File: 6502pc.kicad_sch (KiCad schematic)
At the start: 41 parts, among them J1 DB9 Serial Port, J2 USB_B, J3 Conn_01x08_Pin, J4 Conn_01x08_Pin, J5 Conn_01x16_Socket, J6 SD-Card Board, J7 FTDI Socket, SW1 Reset Switch, SW2 SW_SPST, U1 W65C02SxP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

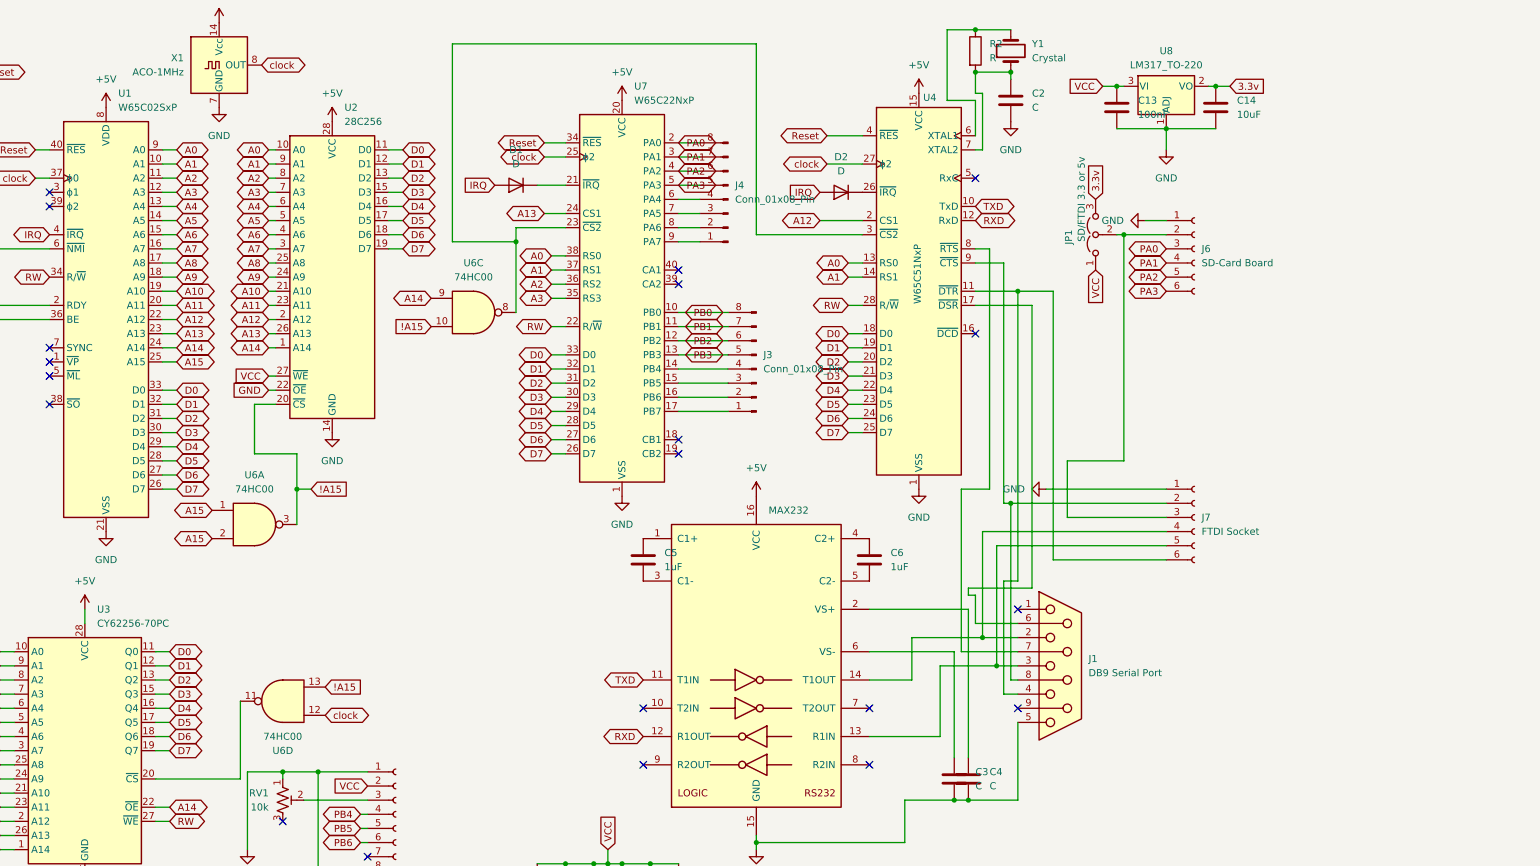
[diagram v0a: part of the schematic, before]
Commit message: Added Expansion
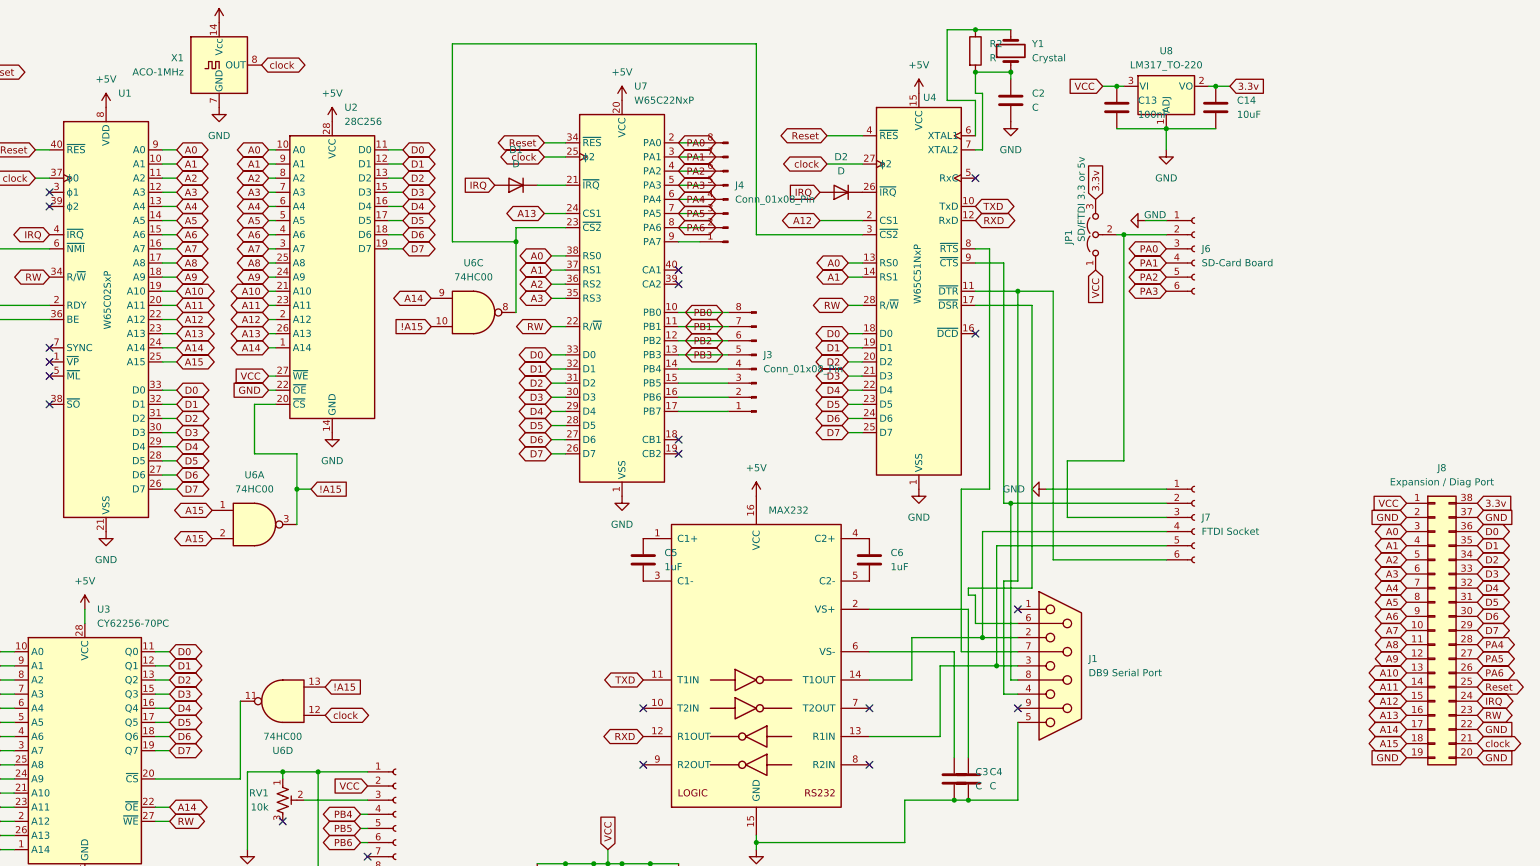
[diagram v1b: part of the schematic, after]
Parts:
- added J8: Expansion / Diag Port, Connector_PinHeader_2.54mm:PinHeader_2x19_P2.54mm_Vertical, symbol Connector_Generic:Conn_02x19_Counter_Clockwise
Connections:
- net +5V: now also J8.1 (Pin_1)
- net 3.3v: now also J8.38 (Pin_38)
- net A0: now also J8.3 (Pin_3)
- net A1: now also J8.4 (Pin_4)
- net A10: now also J8.13 (Pin_13)
- net A11: now also J8.14 (Pin_14)
- net A12: now also J8.15 (Pin_15)
- net A13: now also J8.16 (Pin_16)
- net A14: now also J8.17 (Pin_17)
- net A15: now also J8.18 (Pin_18)
- net A2: now also J8.5 (Pin_5)
- net A3: now also J8.6 (Pin_6)
- net A4: now also J8.7 (Pin_7)
- net A5: now also J8.8 (Pin_8)
- net A6: now also J8.9 (Pin_9)
- net A7: now also J8.10 (Pin_10)
- net A8: now also J8.11 (Pin_11)
- net A9: now also J8.12 (Pin_12)
- net D0: now also J8.36 (Pin_36)
- net D1: now also J8.35 (Pin_35)
- net D2: now also J8.34 (Pin_34)
- net D3: now also J8.33 (Pin_33)
- net D4: now also J8.32 (Pin_32)
- net D5: now also J8.31 (Pin_31)
- net D6: now also J8.30 (Pin_30)
- net D7: now also J8.29 (Pin_29)
- net GND: now also J8.19 (Pin_19), J8.2 (Pin_2), J8.20 (Pin_20), J8.22 (Pin_22), J8.37 (Pin_37)
- net IRQ: now also J8.24 (Pin_24)
- net RW: now also J8.23 (Pin_23)
- net Reset: now also J8.25 (Pin_25)
- net clock: now also J8.21 (Pin_21)
- net PA4: now reaches J4.4 (Pin_4), U7.6 (PA4)
- net PA4: now also J8.28 (Pin_28)
- net PA5: now reaches J4.3 (Pin_3), U7.7 (PA5)
- net PA5: now also J8.27 (Pin_27)
- net PA6: now reaches J4.2 (Pin_2), U7.8 (PA6)
- net PA6: now also J8.26 (Pin_26)

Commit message: Added Expansion
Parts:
- J3, J4: footprint Connector_PinHeader_2.00mm:PinHeader_1x08_P2.00mm_Vertical -> Connector_PinHeader_2.54mm:PinHeader_1x08_P2.54mm_Vertical
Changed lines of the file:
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@@
 			)
 		)
-		(property "Footprint" "Connector_PinHeader_2.00mm:PinHeader_1x08_P2.00mm_Vertical"
+		(property "Footprint" "Connector_PinHeader_2.54mm:PinHeader_1x08_P2.54mm_Vertical"
 			(at 256.54 118.11 0)
 			(effects
@@
 			)
 		)
-		(property "Footprint" "Connector_PinHeader_2.00mm:PinHeader_1x08_P2.00mm_Vertical"
+		(property "Footprint" "Connector_PinHeader_2.54mm:PinHeader_1x08_P2.54mm_Vertical"
 			(at 251.46 87.63 0)
 			(effects

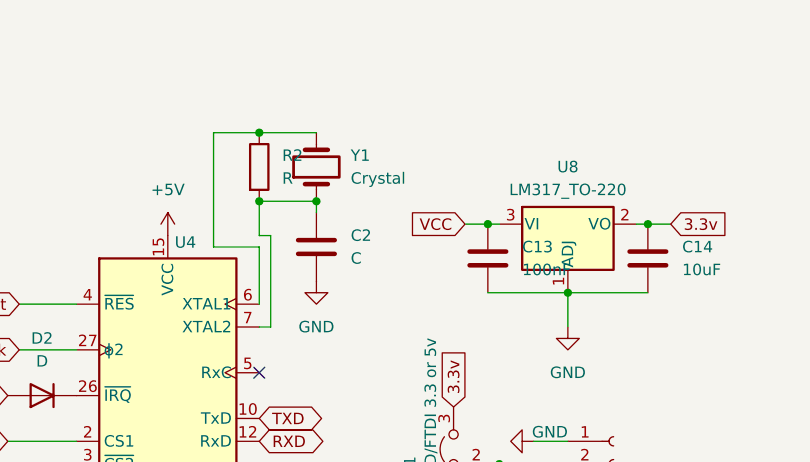
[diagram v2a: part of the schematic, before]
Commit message: Added Expansion
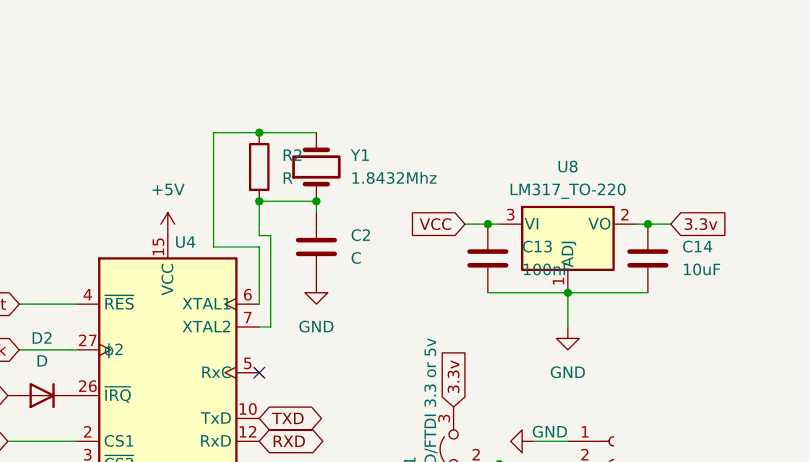
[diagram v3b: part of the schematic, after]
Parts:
- D1, D2: footprint Diode_THT:D_DO-15_P5.08mm_Vertical_AnodeUp -> Resistor_THT:R_Axial_DIN0204_L3.6mm_D1.6mm_P7.62mm_Horizontal
- R3: footprint Resistor_THT:R_Axial_DIN0204_L3.6mm_D1.6mm_P5.08mm_Horizontal -> Resistor_THT:R_Axial_DIN0204_L3.6mm_D1.6mm_P7.62mm_Horizontal
- RV1: footprint Potentiometer_THT:Potentiometer_Runtron_RM-063_Horizontal -> Potentiometer_THT:Potentiometer_Bourns_3296X_Horizontal
- Y1: value Crystal -> 1.8432Mhz; footprint Crystal:Crystal_HC18-U_Horizontal -> Crystal:Crystal_HC18-U_Vertical
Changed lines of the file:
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@@
 			)
 		)
-		(property "Footprint" "Diode_THT:D_DO-15_P5.08mm_Vertical_AnodeUp"
+		(property "Footprint" "Resistor_THT:R_Axial_DIN0204_L3.6mm_D1.6mm_P7.62mm_Horizontal"
 			(at 213.36 85.09 0)
 			(effects
@@
 			)
 		)
-		(property "Footprint" "Diode_THT:D_DO-15_P5.08mm_Vertical_AnodeUp"
+		(property "Footprint" "Resistor_THT:R_Axial_DIN0204_L3.6mm_D1.6mm_P7.62mm_Horizontal"
 			(at 271.78 86.36 0)
 			(effects
@@
 			)
 		)
-		(property "Footprint" "Resistor_THT:R_Axial_DIN0204_L3.6mm_D1.6mm_P5.08mm_Horizontal"
+		(property "Footprint" "Resistor_THT:R_Axial_DIN0204_L3.6mm_D1.6mm_P7.62mm_Horizontal"
 			(at 88.392 167.64 90)
 			(effects
@@
 			)
 		)
-		(property "Footprint" "Potentiometer_THT:Potentiometer_Runtron_RM-063_Horizontal"
+		(property "Footprint" "Potentiometer_THT:Potentiometer_Bourns_3296X_Horizontal"
 			(at 171.45 195.58 0)
 			(effects
@@
 			)
 		)
-		(property "Value" "Crystal"
+		(property "Value" "1.8432Mhz"
 			(at 306.07 62.2299 90)
 			(effects
@@
 			)
 		)
-		(property "Footprint" "Crystal:Crystal_HC18-U_Horizontal"
+		(property "Footprint" "Crystal:Crystal_HC18-U_Vertical"
 			(at 302.26 60.96 0)
 			(effects

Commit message: Added Expansion
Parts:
- J3, J4: footprint Connector_PinHeader_2.54mm:PinHeader_1x08_P2.54mm_Vertical -> Connector_PinSocket_2.54mm:PinSocket_1x08_P2.54mm_Vertical
- J5: footprint Connector_PinHeader_2.54mm:PinHeader_1x16_P2.54mm_Vertical -> Connector_PinSocket_2.54mm:PinSocket_1x16_P2.54mm_Vertical
- J6: footprint Connector_PinHeader_2.54mm:PinHeader_1x06_P2.54mm_Vertical -> Connector_PinSocket_2.54mm:PinSocket_1x06_P2.54mm_Vertical
- J8: footprint Connector_PinHeader_2.54mm:PinHeader_2x19_P2.54mm_Vertical -> Connector_PinSocket_2.54mm:PinSocket_2x19_P2.54mm_Vertical
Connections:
- net PA5: now also J5.4 (Pin_4)
- net PA6: now also J5.5 (Pin_5)
- net PB0: now also J5.7 (Pin_7); no longer J5.11 (Pin_11)
- net PB1: now also J5.8 (Pin_8); no longer J5.12 (Pin_12)
- net PB2: now also J5.9 (Pin_9); no longer J5.13 (Pin_13)
- net PB3: now also J5.10 (Pin_10); no longer J5.14 (Pin_14)
- net PB4: now also J3.4 (Pin_4), J5.11 (Pin_11), U7.14 (PB4); no longer J5.4 (Pin_4)
- net PB5: now also J3.3 (Pin_3), J5.12 (Pin_12), U7.15 (PB5); no longer J5.5 (Pin_5)
- net PB6: now also J3.2 (Pin_2), J5.13 (Pin_13), U7.16 (PB6); no longer J5.6 (Pin_6)
- net PB7: now reaches J3.1 (Pin_1), U7.17 (PB7)
- net PB7: now also J5.14 (Pin_14)
- net PA7: now reaches J4.1 (Pin_1), U7.9 (PA7)
- net PA7: now also J5.6 (Pin_6)
- no-connect marks 28 -> 24
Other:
- note added: "6502 SBC Computer with SD Card / TFDI Serial / DB9 and Expansion Port (Tom Smith)"

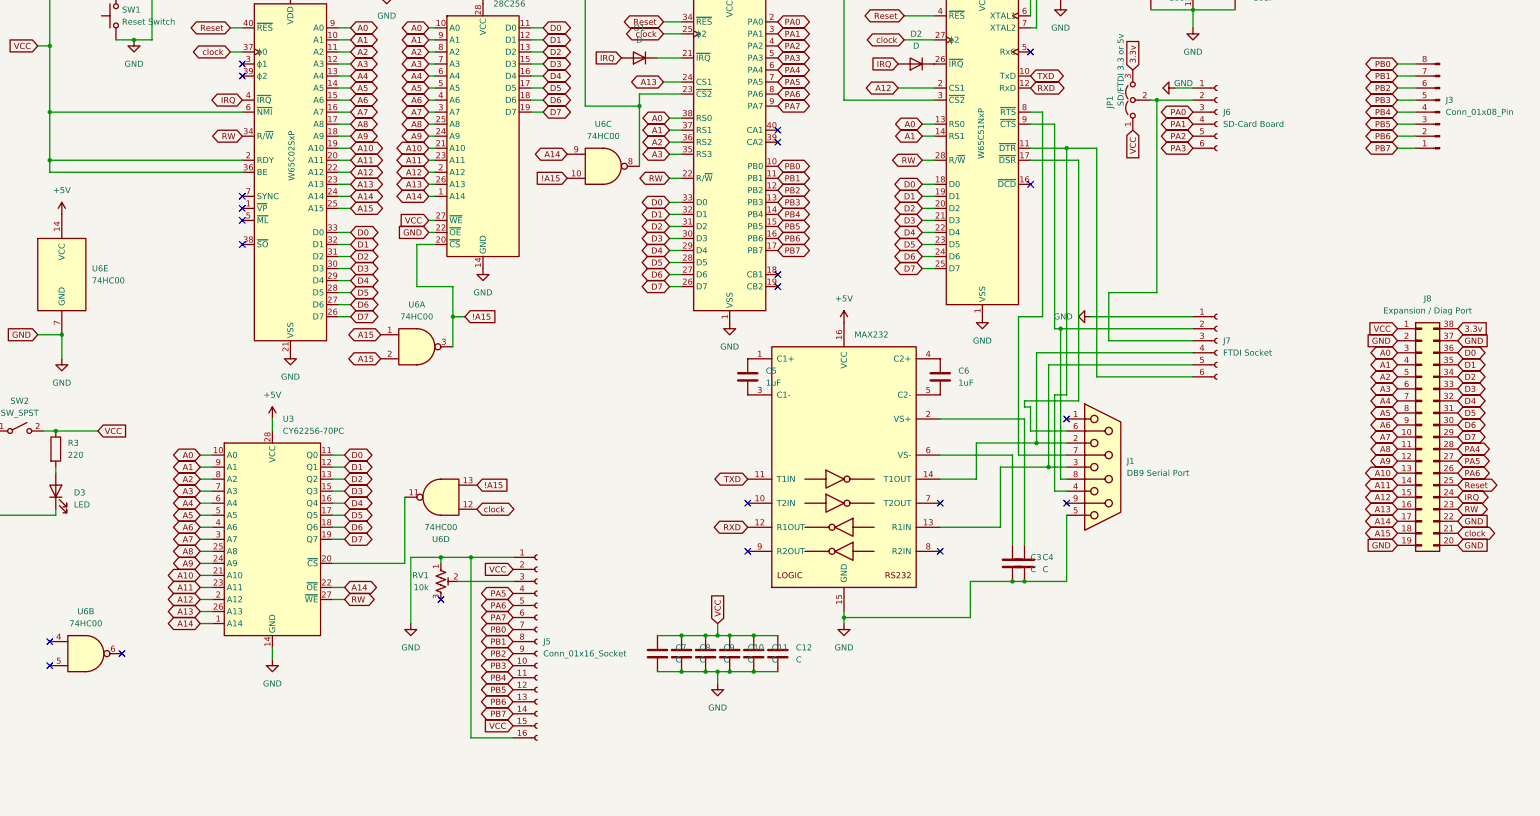
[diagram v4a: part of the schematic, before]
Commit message: Added Expansion
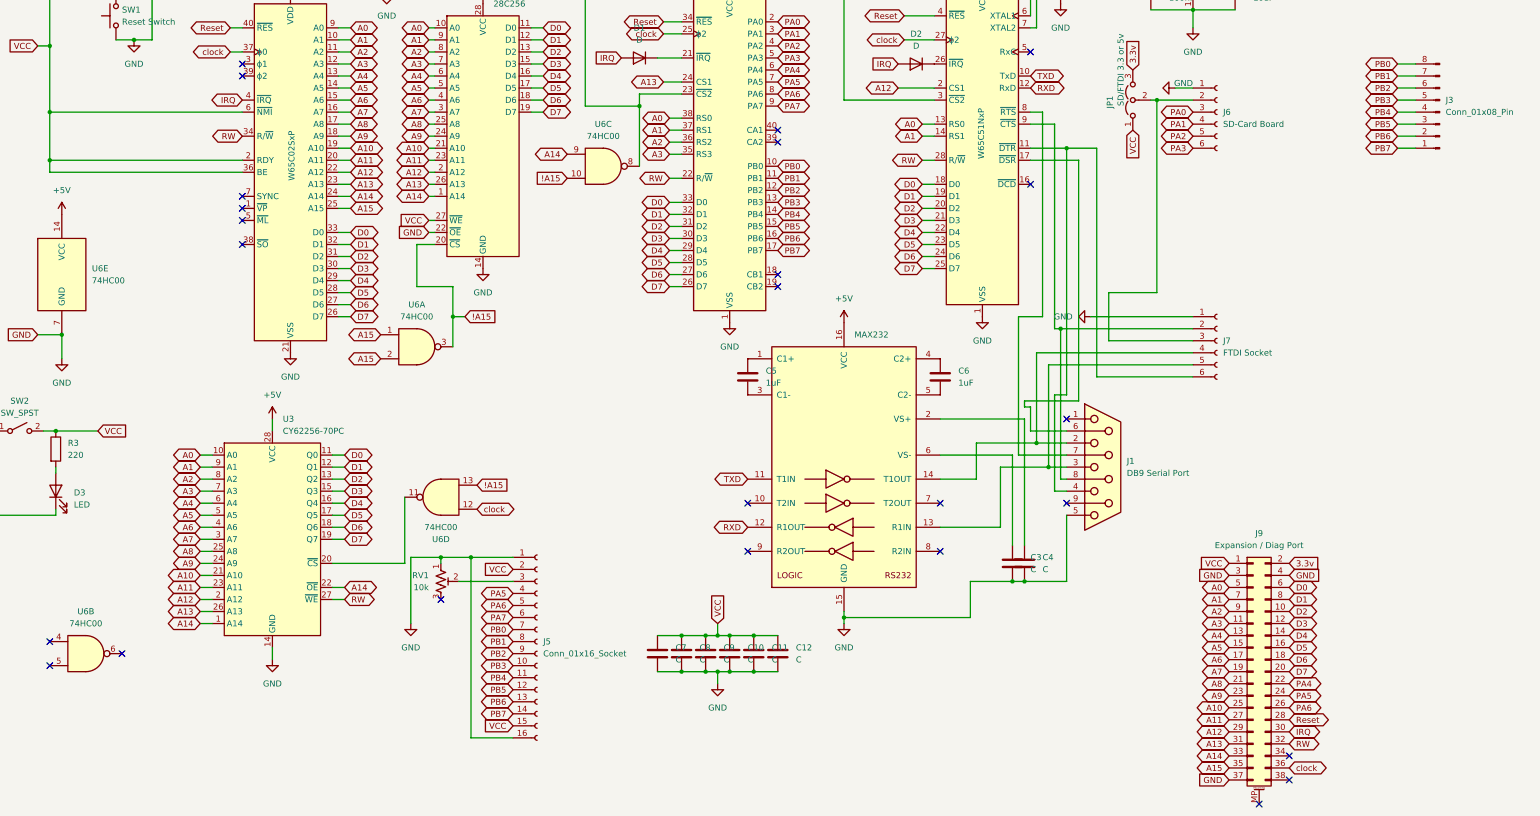
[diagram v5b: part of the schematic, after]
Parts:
- removed J8: Expansion / Diag Port, Connector_PinSocket_2.54mm:PinSocket_2x19_P2.54mm_Vertical, symbol Connector_Generic:Conn_02x19_Counter_Clockwise
- added J9: Expansion / Diag Port, Connector_PinHeader_2.54mm:PinHeader_2x19_P2.54mm_Vertical, symbol Connector_Generic_MountingPin:Conn_02x19_Odd_Even_MountingPin
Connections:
- net +5V: now also J9.1 (Pin_1)
- net 3.3v: now also J9.2 (Pin_2)
- net A0: now also J9.5 (Pin_5)
- net A1: now also J9.7 (Pin_7)
- net A10: now also J9.25 (Pin_25)
- net A11: now also J9.27 (Pin_27)
- net A12: now also J9.29 (Pin_29)
- net A13: now also J9.31 (Pin_31)
- net A14: now also J9.33 (Pin_33)
- net A15: now also J9.35 (Pin_35)
- net A2: now also J9.9 (Pin_9)
- net A3: now also J9.11 (Pin_11)
- net A4: now also J9.13 (Pin_13)
- net A5: now also J9.15 (Pin_15)
- net A6: now also J9.17 (Pin_17)
- net A7: now also J9.19 (Pin_19)
- net A8: now also J9.21 (Pin_21)
- net A9: now also J9.23 (Pin_23)
- net D0: now also J9.6 (Pin_6)
- net D1: now also J9.8 (Pin_8)
- net D2: now also J9.10 (Pin_10)
- net D3: now also J9.12 (Pin_12)
- net D4: now also J9.14 (Pin_14)
- net D5: now also J9.16 (Pin_16)
- net D6: now also J9.18 (Pin_18)
- net D7: now also J9.20 (Pin_20)
- net GND: now also J9.3 (Pin_3), J9.37 (Pin_37), J9.4 (Pin_4)
- net IRQ: now also J9.30 (Pin_30)
- net PA4: now also J9.22 (Pin_22)
- net PA5: now also J9.24 (Pin_24)
- net PA6: now also J9.26 (Pin_26)
- net RW: now also J9.32 (Pin_32)
- net Reset: now also J9.28 (Pin_28)
- net clock: now also J9.36 (Pin_36)
- no-connect marks 24 -> 27

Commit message: Routing and added auto reset
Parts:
- added SW3: Reset Switch, Button_Switch_THT:SW_PUSH_6mm, symbol Switch:SW_Push
- added U9: DS1813-10, 21-0248A_MXM, symbol 2025-06-11_10-50-45:DS1813-10
- C13, C14: footprint Capacitor_THT:C_Radial_D8.0mm_H11.5mm_P3.50mm -> Capacitor_THT:C_Disc_D10.0mm_W2.5mm_P5.00mm
- J1: footprint Connector_Dsub:DSUB-9_Male_Horizontal_P2.77x2.84mm_EdgePinOffset4.94mm_Housed_MountingHolesOffset4.94mm -> DSUB-9_Female_Horizontal_P2.77x2.84mm_EdgePinOffset7.70mm_Housed_MountingHolesOffset9.12mm
- J3: value Conn_01x08_Pin -> Port B
- J4: value Conn_01x08_Pin -> Port A
- J5: value Conn_01x16_Socket -> Display Connector
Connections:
- net +5V: now also U9.2 (VCC)
- net GND: now also SW3.1, U9.3 (GND)
- net Reset: now also SW3.2, U9.1 (~R~~S~~T~)

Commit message: bom and sound app
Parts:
- J9: footprint Connector_PinHeader_2.54mm:PinHeader_2x19_P2.54mm_Vertical -> Connector_PinSocket_2.54mm:PinSocket_2x19_P2.54mm_Vertical
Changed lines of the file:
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@@
 			)
 		)
-		(property "Footprint" "Connector_PinHeader_2.54mm:PinHeader_2x19_P2.54mm_Vertical"
+		(property "Footprint" "Connector_PinSocket_2.54mm:PinSocket_2x19_P2.54mm_Vertical"
 			(at 342.9 214.63 0)
 			(effects
